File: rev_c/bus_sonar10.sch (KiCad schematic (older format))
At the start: 39 parts, among them J1 TERMINATE_JUMPER, SW1 MJTP1243, U1 74HCT08, U2 LM2940, U3 MCP2562, U4 ATMEGA328_DIP28, U5 74HCT32, X1 16MHz

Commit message: Wrapped up Rev. C
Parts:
- added R10: 100K, bus_sonar10:Pin_Header_Straight_1x09, symbol R_VERT_SIP9
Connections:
- net D12: now also R10.2
- net GND: now also R10.1, R10.1, R10.1, R10.1, R10.1, R10.1, R10.1, R10.1
- net at N3.11 (ECHO2), U5.2: now also R10.3
- net at N3.3 (ECHO1), U5.1: now also R10.5
- net at N3.35 (ECHO5), U5.5: now also R10.4
- net at N4.11 (ECHO2), U5.13: now also R10.6
- net at N4.27 (ECHO4), U5.9: now also R10.9
- net at N4.3 (ECHO1), U5.12: now also R10.7
- net at N4.35 (ECHO5), U5.10: now also R10.8
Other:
- moved on the sheet: U5A, U5C, U5D

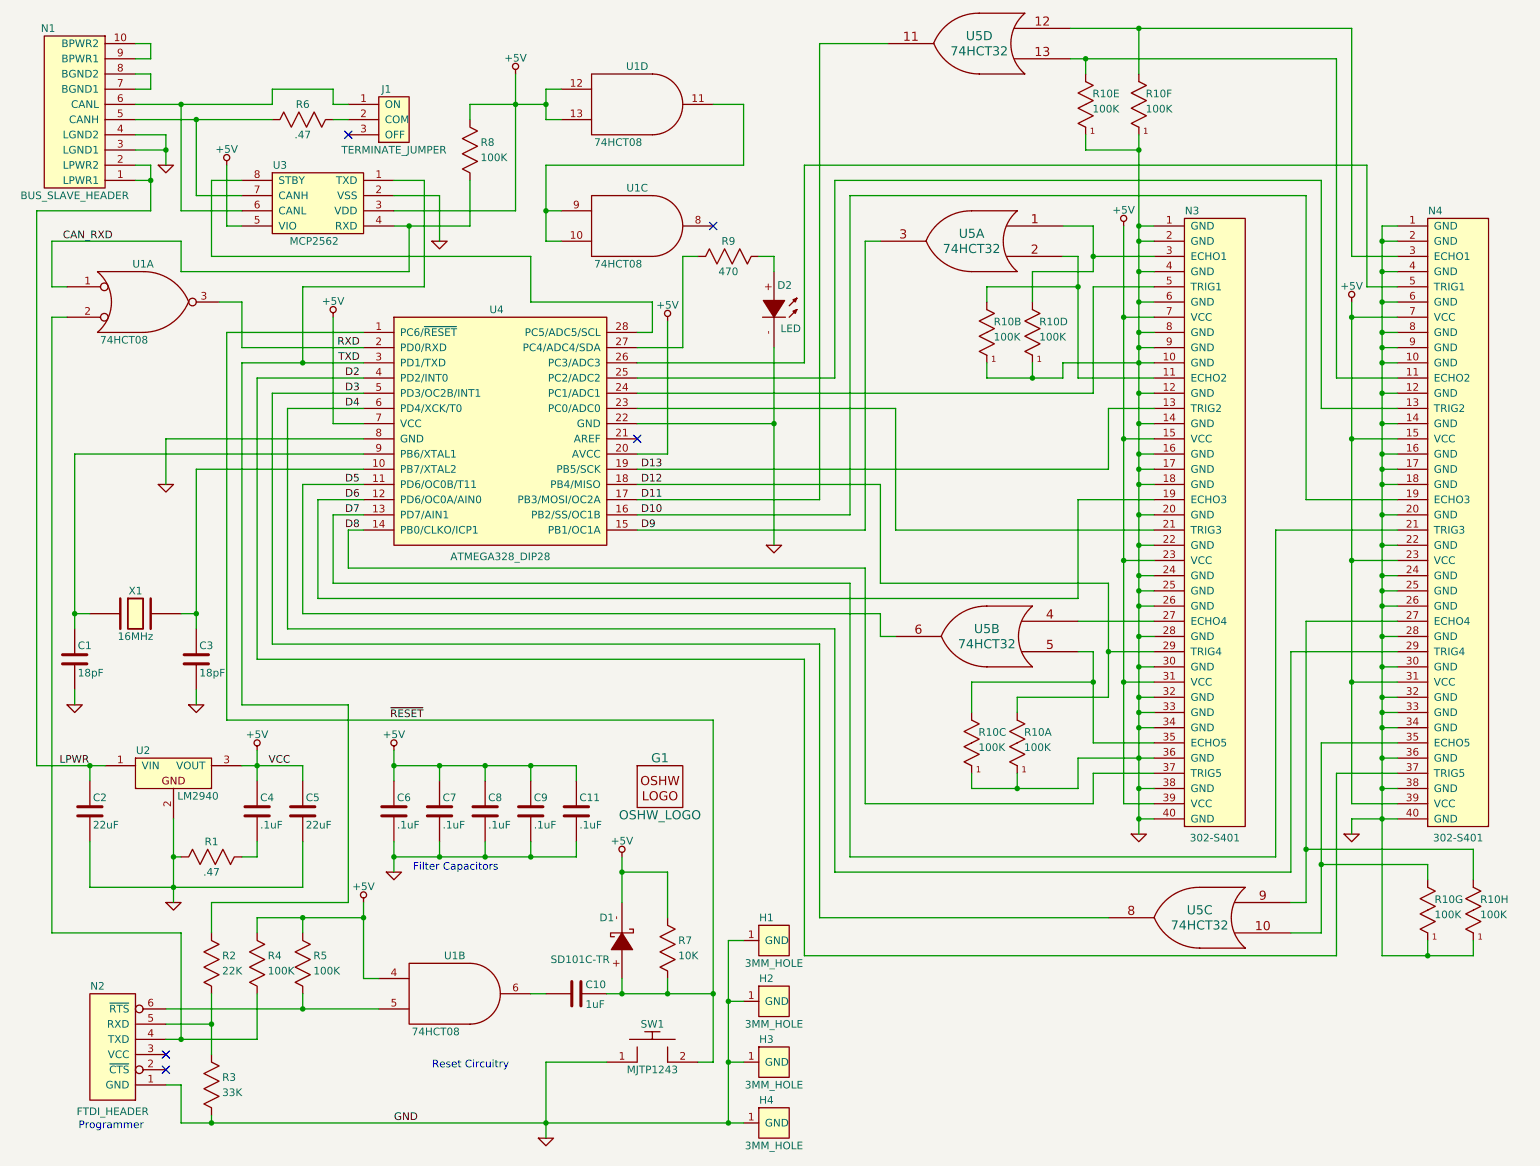
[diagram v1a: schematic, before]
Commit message: Changed 8 100K's to 8 100Kx8's.
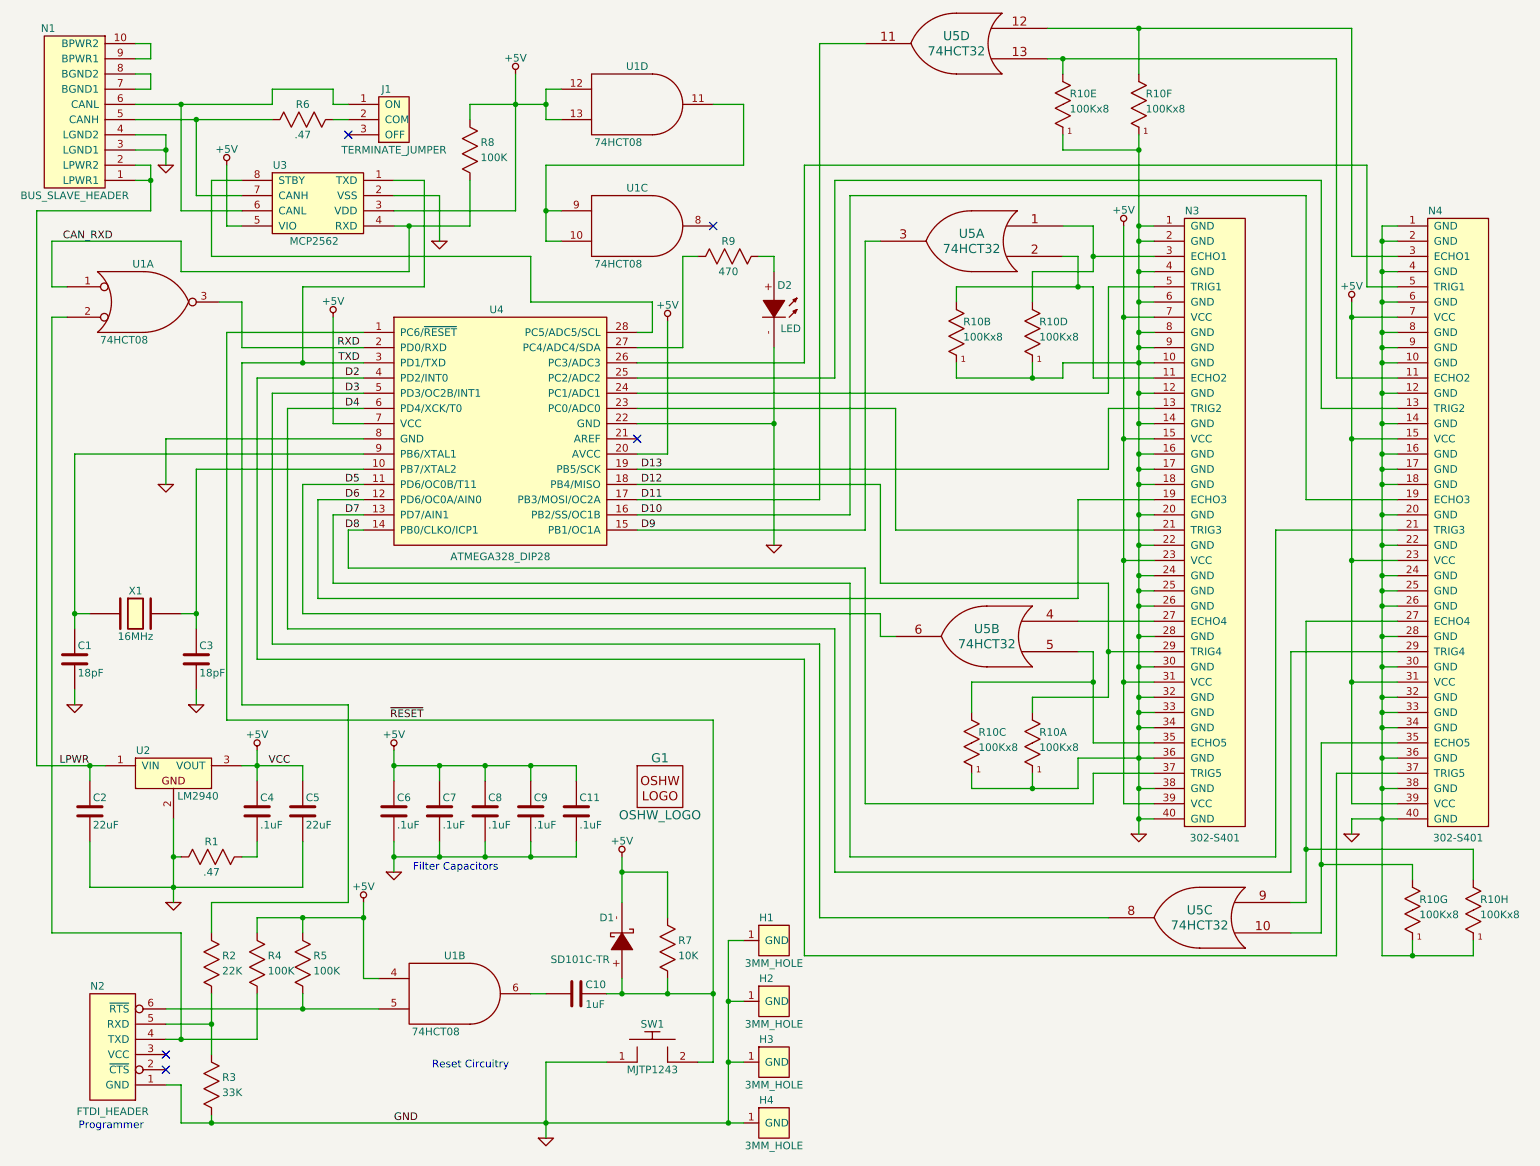
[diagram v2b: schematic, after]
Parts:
- R10: value 100K -> 100Kx8
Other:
- moved on the sheet: R10A, R10B, R10E, R10G, U5D
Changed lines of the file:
@@
 L 74LS32 U5
 U 4 1 53F1905D
-P 6850 700
-F 0 "U5" H 6850 750 60  0000 C CNN
-F 1 "74HCT32" H 6850 650 60  0000 C CNN
-F 2 "bus_sonar10:DIP-14__300" H 6850 700 60  0001 C CNN
-F 3 "" H 6850 700 60  0000 C CNN
-	4    6850 700
+P 6700 700
+F 0 "U5" H 6700 750 60  0000 C CNN
+F 1 "74HCT32" H 6700 650 60  0000 C CNN
+F 2 "bus_sonar10:DIP-14__300" H 6700 700 60  0001 C CNN
+F 3 "" H 6700 700 60  0000 C CNN
+	4    6700 700
 	-1   0    0    -1
 $EndComp
@@
 L R_VERT_SIP9 R10
 U 7 1 54412CC5
-P 9800 6400
-F 0 "R10" H 9845 6470 50  0000 L CNN
-F 1 "100K" H 9845 6370 50  0000 L CNN
-F 2 "bus_sonar10:Pin_Header_Straight_1x09" H 9800 6400 50  0001 C CNN
-F 3 "" H 9800 6400 50  0000 C CNN
-	7    9800 6400
+P 9700 6400
+F 0 "R10" H 9745 6470 50  0000 L CNN
+F 1 "100Kx8" H 9745 6370 50  0000 L CNN
+F 2 "bus_sonar10:Pin_Header_Straight_1x09" H 9700 6400 50  0001 C CNN
+F 3 "" H 9700 6400 50  0000 C CNN
+	7    9700 6400
 	1    0    0    -1
 $EndComp
@@
 P 10100 6400
 F 0 "R10" H 10145 6470 50  0000 L CNN
-F 1 "100K" H 10145 6370 50  0000 L CNN
+F 1 "100Kx8" H 10145 6370 50  0000 L CNN
 F 2 "bus_sonar10:Pin_Header_Straight_1x09" H 10100 6400 50  0001 C CNN
 F 3 "" H 10100 6400 50  0000 C CNN
@@
 L R_VERT_SIP9 R10
 U 1 1 544140EE
-P 7100 5300
-F 0 "R10" H 7145 5370 50  0000 L CNN
-F 1 "100K" H 7145 5270 50  0000 L CNN
-F 2 "bus_sonar10:Pin_Header_Straight_1x09" H 7100 5300 50  0001 C CNN
-F 3 "" H 7100 5300 50  0000 C CNN
-	1    7100 5300
+P 7200 5300
+F 0 "R10" H 7245 5370 50  0000 L CNN
+F 1 "100Kx8" H 7245 5270 50  0000 L CNN
+F 2 "bus_sonar10:Pin_Header_Straight_1x09" H 7200 5300 50  0001 C CNN
+F 3 "" H 7200 5300 50  0000 C CNN
+	1    7200 5300
 	1    0    0    -1
 $EndComp
@@
 P 6800 5300
 F 0 "R10" H 6845 5370 50  0000 L CNN
-F 1 "100K" H 6845 5270 50  0000 L CNN
+F 1 "100Kx8" H 6845 5270 50  0000 L CNN
 F 2 "bus_sonar10:Pin_Header_Straight_1x09" H 6800 5300 50  0001 C CNN
 F 3 "" H 6800 5300 50  0000 C CNN
@@
 L R_VERT_SIP9 R10
 U 5 1 54416A05
-P 7550 1100
-F 0 "R10" H 7595 1170 50  0000 L CNN
-F 1 "100K" H 7595 1070 50  0000 L CNN
-F 2 "bus_sonar10:Pin_Header_Straight_1x09" H 7550 1100 50  0001 C CNN
-F 3 "" H 7550 1100 50  0000 C CNN
-	5    7550 1100
+P 7400 1100
+F 0 "R10" H 7445 1170 50  0000 L CNN
+F 1 "100Kx8" H 7445 1070 50  0000 L CNN
+F 2 "bus_sonar10:Pin_Header_Straight_1x09" H 7400 1100 50  0001 C CNN
+F 3 "" H 7400 1100 50  0000 C CNN
+	5    7400 1100
 	1    0    0    -1
 $EndComp
@@
 P 7900 1100
 F 0 "R10" H 7945 1170 50  0000 L CNN
-F 1 "100K" H 7945 1070 50  0000 L CNN
+F 1 "100Kx8" H 7945 1070 50  0000 L CNN
 F 2 "bus_sonar10:Pin_Header_Straight_1x09" H 7900 1100 50  0001 C CNN
 F 3 "" H 7900 1100 50  0000 C CNN
@@
 L R_VERT_SIP9 R10
 U 2 1 54418077
-P 6900 2600
-F 0 "R10" H 6945 2670 50  0000 L CNN
-F 1 "100K" H 6945 2570 50  0000 L CNN
-F 2 "bus_sonar10:Pin_Header_Straight_1x09" H 6900 2600 50  0001 C CNN
-F 3 "" H 6900 2600 50  0000 C CNN
-	2    6900 2600
+P 6700 2600
+F 0 "R10" H 6745 2670 50  0000 L CNN
+F 1 "100Kx8" H 6745 2570 50  0000 L CNN
+F 2 "bus_sonar10:Pin_Header_Straight_1x09" H 6700 2600 50  0001 C CNN
+F 3 "" H 6700 2600 50  0000 C CNN
+	2    6700 2600
 	1    0    0    -1
 $EndComp
@@
 P 7200 2600
 F 0 "R10" H 7245 2670 50  0000 L CNN
-F 1 "100K" H 7245 2570 50  0000 L CNN
+F 1 "100Kx8" H 7245 2570 50  0000 L CNN
 F 2 "bus_sonar10:Pin_Header_Straight_1x09" H 7200 2600 50  0001 C CNN
 F 3 "" H 7200 2600 50  0000 C CNN
@@
 	2200 4650 2200 3000
 Wire Wire Line
-	7600 3000 4600 3000
+	7700 3000 4600 3000
 Wire Wire Line
 	2600 3800 2600 4250
@@
 	9600 2100 9300 2100
 Wire Wire Line
-	9300 2100 9300 600
-Wire Wire Line
-	9300 600  7450 600
+	9300 600  9300 2100
+Wire Wire Line
+	7300 600  9300 600
 Wire Wire Line
 	9600 2900 9200 2900
 Wire Wire Line
-	9200 2900 9200 800
-Wire Wire Line
-	9200 800  7450 800
+	9200 800  9200 2900
+Wire Wire Line
+	7300 800  9200 800
 Wire Wire Line
 	9600 1900 9500 1900
@@
 Connection ~ 9500 2000
 Wire Wire Line
-	9600 2200 9500 2200
+	9500 2200 9600 2200
 Connection ~ 9500 2200
 Wire Wire Line
@@
 Connection ~ 9500 2400
 Wire Wire Line
-	9600 2600 9500 2600
+	9500 2600 9600 2600
 Connection ~ 9500 2600
 Wire Wire Line
-	9600 2700 9500 2700
+	9500 2700 9600 2700
 Connection ~ 9500 2700
 Wire Wire Line
-	9600 2800 9500 2800
+	9500 2800 9600 2800
 Connection ~ 9500 2800
 Wire Wire Line
-	9600 3000 9500 3000
+	9500 3000 9600 3000
 Connection ~ 9500 3000
 Wire Wire Line
-	9600 3200 9500 3200
+	9500 3200 9600 3200
 Connection ~ 9500 3200
 Wire Wire Line
-	9600 3400 9500 3400
+	9500 3400 9600 3400
 Connection ~ 9500 3400
 Wire Wire Line
-	9600 3500 9500 3500
+	9500 3500 9600 3500
 Connection ~ 9500 3500
 Wire Wire Line
-	9600 3600 9500 3600
+	9500 3600 9600 3600
 Connection ~ 9500 3600
 Wire Wire Line
-	9600 3800 9500 3800
+	9500 3800 9600 3800
 Connection ~ 9500 3800
 Wire Wire Line
-	9600 4000 9500 4000
+	9500 4000 9600 4000
 Connection ~ 9500 4000
 Wire Wire Line
-	9600 4200 9500 4200
+	9500 4200 9600 4200
 Connection ~ 9500 4200
 Wire Wire Line
-	9600 4300 9500 4300
+	9500 4300 9600 4300
 Connection ~ 9500 4300
 Wire Wire Line
-	9600 4600 9500 4600
+	9500 4600 9600 4600
 Connection ~ 9500 4600
 Wire Wire Line
-	9600 4800 9500 4800
+	9500 4800 9600 4800
 Connection ~ 9500 4800
 Wire Wire Line
-	9600 5000 9500 5000
+	9500 5000 9600 5000
 Connection ~ 9500 5000
 Wire Wire Line
-	9600 5100 9500 5100
+	9500 5100 9600 5100
 Connection ~ 9500 5100
 Wire Wire Line
-	9600 5200 9500 5200
+	9500 5200 9600 5200
 Connection ~ 9500 5200
 Wire Wire Line
-	9600 5400 9500 5400
+	9500 5400 9600 5400
 Connection ~ 9500 5400
 Wire Wire Line
-	9600 5600 9500 5600
+	9500 5600 9600 5600
 Connection ~ 9500 5600
 Wire Wire Line
@@
 Connection ~ 7900 5800
 Wire Wire Line
-	6250 700  5800 700
+	6100 700  5800 700
 Wire Wire Line
 	6200 3600 4600 3600
@@
 	5800 4650 5800 6450
 Wire Wire Line
-	7500 2900 8000 2900
-Wire Wire Line
-	7500 2100 7500 2900
+	7600 2900 8000 2900
+Wire Wire Line
+	7500 2100 7500 2300
 Wire Wire Line
 	7500 2100 7400 2100
@@
 	7700 3100 7700 3500
 Wire Wire Line
-	8000 2300 7600 2300
-Wire Wire Line
-	7600 2300 7600 3000
+	8000 2300 7700 2300
+Wire Wire Line
+	7700 2300 7700 3000
 Wire Wire Line
 	4600 2900 5900 2900
@@
 	9300 2400 9300 5700
 Wire Wire Line
-	9600 4400 9500 4400
+	9500 4400 9600 4400
 Connection ~ 9500 4400
 Wire Wire Line
@@
 	10100 6700 10100 6600
 Wire Wire Line
-	9800 6700 9800 6600
-Wire Wire Line
-	9800 6200 9800 6100
+	9700 6700 9700 6600
+Wire Wire Line
+	9700 6200 9700 6100
 Wire Wire Line
 	10100 6200 10100 6000
-Connection ~ 9800 6700
+Connection ~ 9700 6700
 Wire Wire Line
 	8000 5500 7600 5500
@@
 Connection ~ 7600 4900
 Wire Wire Line
-	7700 5000 7100 5000
+	7700 5000 7200 5000
 Connection ~ 7700 4700
 Wire Wire Line
@@
 	7500 5600 7500 5400
 Wire Wire Line
-	7100 5500 7100 5600
-Connection ~ 7100 5600
-Wire Wire Line
-	7550 1300 7550 1400
-Wire Wire Line
-	7550 1400 7900 1400
-Wire Wire Line
-	7550 900  7550 800
-Connection ~ 7550 800
+	7200 5500 7200 5600
+Connection ~ 7200 5600
+Wire Wire Line
+	7400 1300 7400 1400
+Wire Wire Line
+	7400 1400 7900 1400
+Wire Wire Line
+	7400 900  7400 800
+Connection ~ 7400 800
 Wire Wire Line
 	7900 900  7900 600
@@
 	7200 2200 7200 2400
 Wire Wire Line
-	7500 2300 6900 2300
-Wire Wire Line
-	6900 2300 6900 2400
+	6700 2300 7600 2300
+Wire Wire Line
+	6700 2300 6700 2400
 Connection ~ 7500 2300
 Wire Wire Line
-	6900 2800 6900 2900
-Wire Wire Line
-	6900 2900 7400 2900
+	6700 2800 6700 2900
+Wire Wire Line
+	6700 2900 7400 2900
 Wire Wire Line
 	7200 2900 7200 2800
@@
 	9200 5500 9200 6700
 Wire Wire Line
-	9800 6100 9100 6100
+	9700 6100 9100 6100
 Connection ~ 9100 6100
 Wire Wire Line
@@
 	6800 5100 6800 4900
 Wire Wire Line
-	7100 5000 7100 5100
+	7200 5000 7200 5100
+Wire Wire Line
+	7600 2300 7600 2900
 $EndSCHEMATC
